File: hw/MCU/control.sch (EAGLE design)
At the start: 24 parts, among them J1 MAGJACK, U1 ATMEGA328P, U2 W5500, U3 TC7SU04F

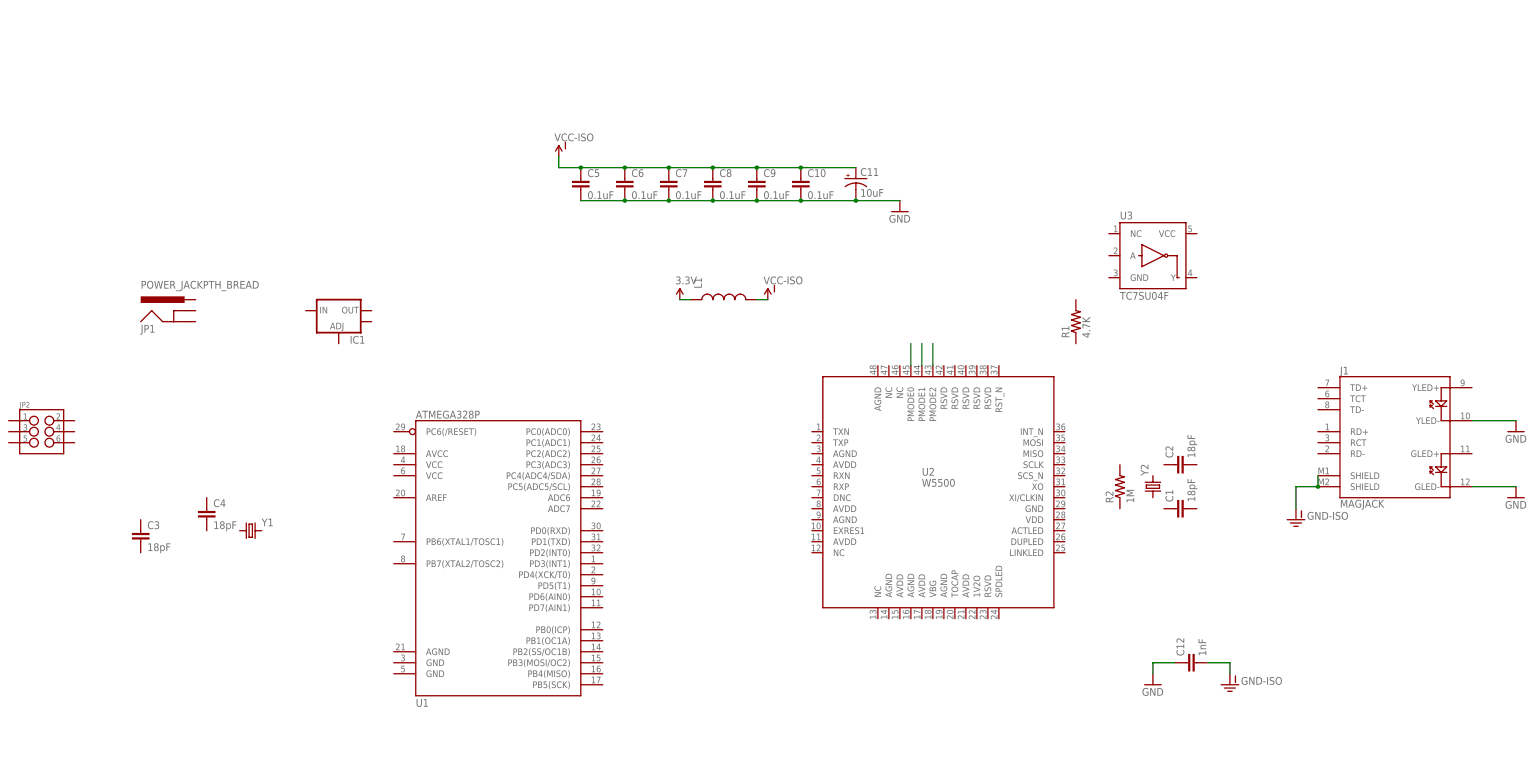
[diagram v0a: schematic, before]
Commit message: Added power indication LED and Battery current/voltage measurement to output board. Added atmega32u2, IMU header, Temp sensor connector, and wiz55io header to control board.
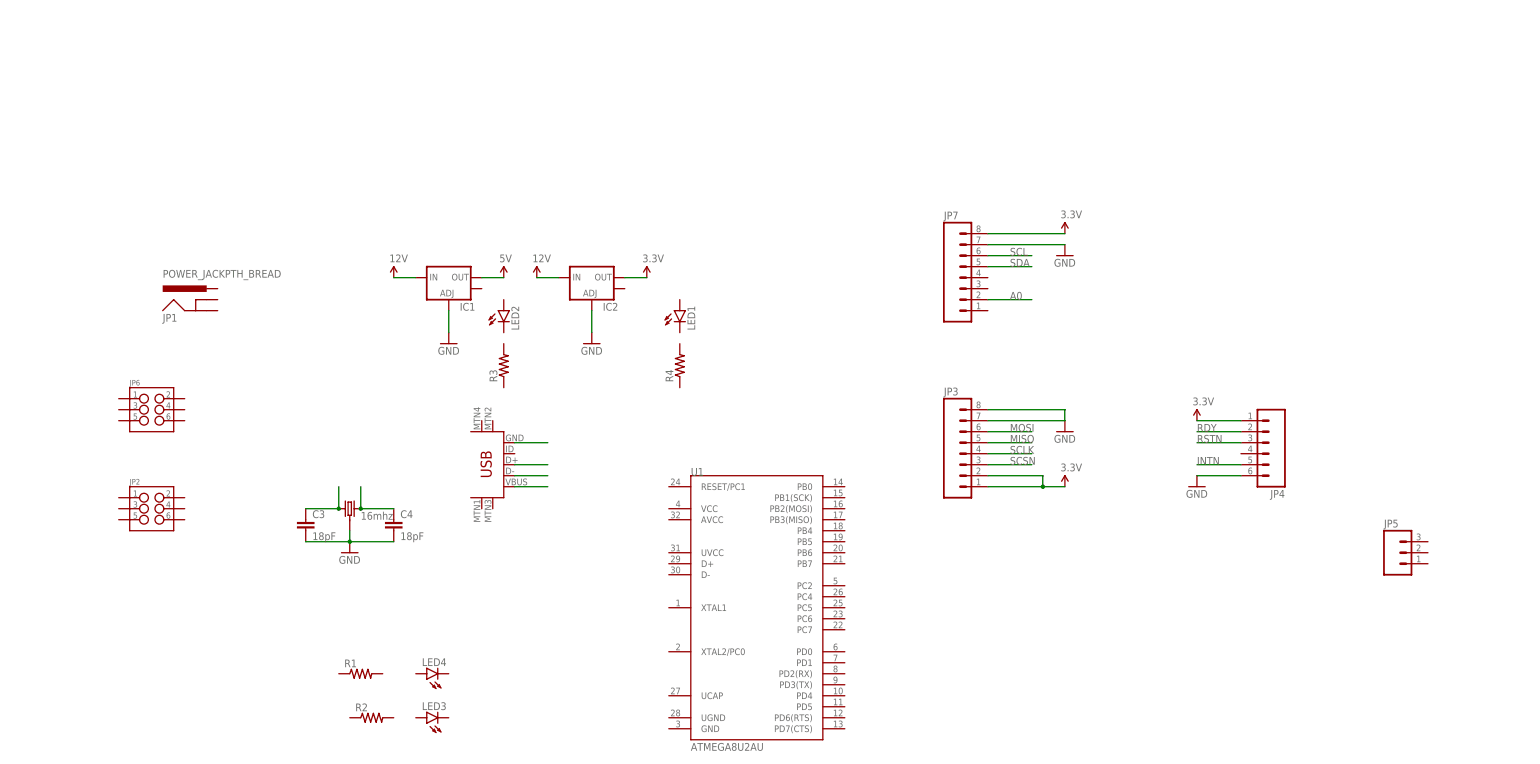
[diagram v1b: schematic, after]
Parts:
- removed C1, C2: 18pF, SparkFun-Capacitors:18PF-50V-5%(0603)
- removed C10, C5, C6, C7, C8, C9: 0.1uF, SparkFun-Capacitors:0.1UF-25V-5%(0603)
- removed C11: 10uF, SparkFun-Capacitors:10UF-16V-10%(TANT)
- removed C12: 1nF, SparkFun-Capacitors:1NF/1000PF-50V-10%(0603)
- removed J1: MAGJACK, SparkFun-Connectors:MAGJACK
- removed L1: (no value), SparkFun-Passives:INDUCTOR0603
- removed U2: W5500, W5500:W5500
- removed U3: TC7SU04F, SparkFun-DigitalIC:INVERTER_SOT23-5
- removed Y1, Y2: (no value), SparkFun-FreqCtrl:CRYSTALHC49US
- added IC2: (no value), SparkFun-PowerIC:V_REG_LM1117SOT223
- added JP3, JP7: (no value), SparkFun-Connectors:M08
- added JP4: (no value), SparkFun-Connectors:M06SILK_FEMALE_PTH
- added JP5: (no value), SparkFun-Connectors:M03PTH
- added JP6: (no value), SparkFun-Connectors:M03X2SHROUD
- added LED1, LED2, LED3, LED4: (no value), SparkFun-LED:LED0603
- added R3, R4: (no value), SparkFun-Passives:RESISTOR0603-RES
- added U$3: 16mhz, SparkFun-FreqCtrl:CRYSTAL-GROUNDED
- added U$5: USB-MINIB-5PIN, SparkFun-Connectors:USB-MINIB-5PIN
- R1: value 4.7K -> (none); device SparkFun-Resistors:4.7KOHM-1/10W-1%(0603) -> SparkFun-Passives:RESISTOR0603-RES
- R2: value 1M -> (none); device SparkFun-Resistors:1MOHM-1/10W-1%(0603) -> SparkFun-Passives:RESISTOR0603-RES
- U1: value ATMEGA328P -> ATMEGA8U2AU; device SparkFun-DigitalIC:ATMEGA328_SMT -> SparkFun-DigitalIC:ATMEGA8U2AU
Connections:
- removed net GND-ISO: C12.2, J1.SHIELD@0, J1.SHIELD@1
- removed net N$4: U2.PMODE0
- removed net N$5: U2.PMODE1
- removed net N$6: U2.PMODE2
- removed net VCC-ISO: C10.1, C11.+, C5.1, C6.1, C7.1, C8.1, C9.1, L1.2
- new net 12V: IC1.IN, IC2.IN
- new net 5V: IC1.OUT
- new net A0: JP7.2
- new net INTN: JP4.5
- new net MISO: JP3.5
- new net MOSI: JP3.6
- new net N$1: JP3.7, JP3.8
- new net N$10: U$5.VBUS
- new net N$2: C3.1, U$3.1
- new net N$3: C4.1, U$3.2
- new net N$7: U$5.GND
- new net N$8: U$5.D+
- new net N$9: U$5.D-
- new net RDY: JP4.2
- new net RSTN: JP4.3
- new net SCL: JP7.6
- new net SCLK: JP3.4
- new net SCSN: JP3.3
- new net SDA: JP7.5
- net 3.3V: now also IC2.OUT, JP3.1, JP3.2, JP4.1, JP7.8; no longer L1.1
- net GND: now also C3.2, C4.2, IC1.ADJ, IC2.ADJ, JP4.6, JP7.7, U$3.3; no longer C10.2, C11.-, C12.1, C5.2, C6.2, C7.2, C8.2, C9.2, J1.GLED-, J1.YLED-
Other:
- moved on the sheet: C3, C4, IC1, JP1, JP2, R1, R2

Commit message: Laid out positions of components on board.
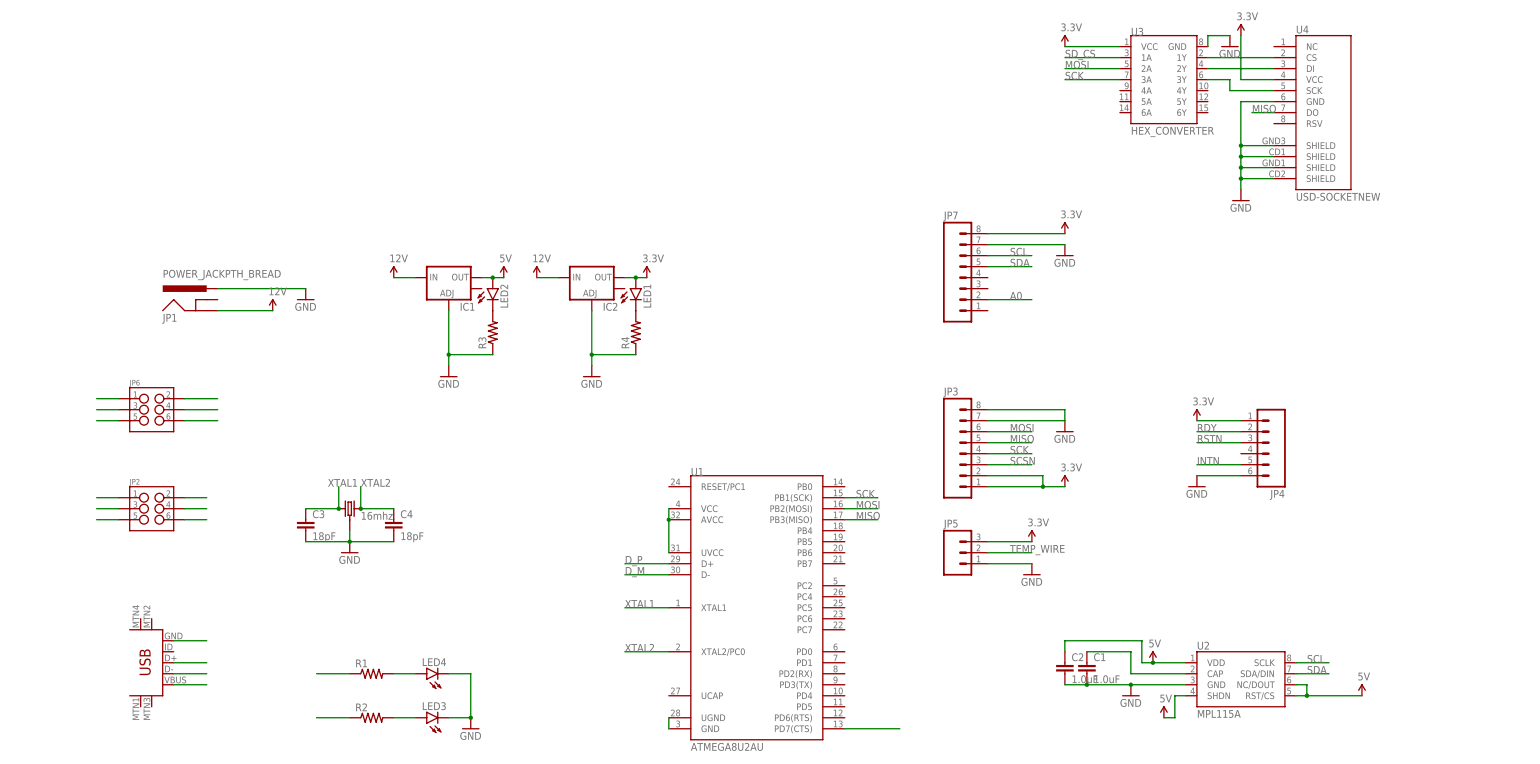
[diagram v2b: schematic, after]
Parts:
- added C1, C2: 1.0uF, SparkFun-Capacitors:1.0UF-16V-10%(0603)
- added U2: MPL115A, SparkFun-Sensors:MPL115A
- added U3: HEX_CONVERTER, SparkFun-DigitalIC:HEX_CONVERTER
- added U4: USD-SOCKETNEW, SparkFun-Connectors:USD-SOCKETNEW
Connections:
- removed net SCLK: JP3.4
- new net D_M: U1.D-
- new net D_P: U1.D+
- new net N$11: U3.2Y, U4.DI
- new net N$12: U3.3Y, U4.SCK
- new net N$15: C1.1, U2.CAP
- new net N$16: R1.1
- new net N$17: R2.1
- new net N$18: JP2.6
- new net N$19: JP2.4
- new net N$20: JP2.2
- new net N$21: JP2.1
- new net N$22: JP2.3
- new net N$23: JP2.5
- new net N$24: JP6.5
- new net N$25: JP6.3
- new net N$26: JP6.1
- new net N$27: JP6.2
- new net N$28: JP6.4
- new net N$29: JP6.6
- new net N$30: U1.GND, U1.UGND
- new net N$31: U1.AVCC, U1.UVCC, U1.VCC
- new net N$32: U1.PD7(CTS)
- new net N$4: LED2.C, R3.2
- new net N$5: LED1.C, R4.2
- new net N$6: U3.1Y, U4.CS
- new net SCK: JP3.4, U1.PB1(SCK), U3.3A
- new net SD_CS: U3.1A
- new net TEMP_WIRE: JP5.2
- new net XTAL1: C3.1, U$3.1, U1.XTAL1
- new net XTAL2: C4.1, U$3.2, U1.XTAL2/PC0
- net 12V: now also JP1.GND
- net 3.3V: now also JP5.3, LED1.A, U3.VCC, U4.VCC
- net 5V: now also C2.1, LED2.A, U2.NC/DOUT, U2.RST/CS, U2.SHDN, U2.VDD
- net GND: now also C1.2, C2.2, JP1.PWR, JP5.1, LED3.C, LED4.C, R3.1, R4.1, U2.GND, U3.GND, U4.GND, U4.SHIELD@1, U4.SHIELD@2, U4.SHIELD@3, U4.SHIELD@4
- net MISO: now also U1.PB3(MISO), U4.DO
- net MOSI: now also U1.PB2(MOSI), U3.2A
- net N$2: now also LED4.A, R1.2; no longer C3.1, U$3.1
- net N$3: now also LED3.A, R2.2; no longer C4.1, U$3.2
- net SCL: now also U2.SCLK
- net SDA: now also U2.SDA/DIN
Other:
- moved on the sheet: JP5, LED1, LED2, R1, R3, R4
